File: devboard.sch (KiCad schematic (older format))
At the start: 101 parts, among them J1 Conn_01x04, J2 Conn_02x05_Odd_Even, J3 USB_B_Micro, J4 Conn_01x04, J5 Conn_02x10_Counter_Clockwise, J6 Conn_02x04_Counter_Clockwise, Q1 Q_NPN_BEC, Q2 Q_NPN_BEC, SW1 SW_SPST, U1 ATmega128L-8AU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

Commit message: Schematic cohesion improvements
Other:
- note added: "Daniel A. Stutman - 2021"
- note removed: "Daniel A. Stutman -2021"

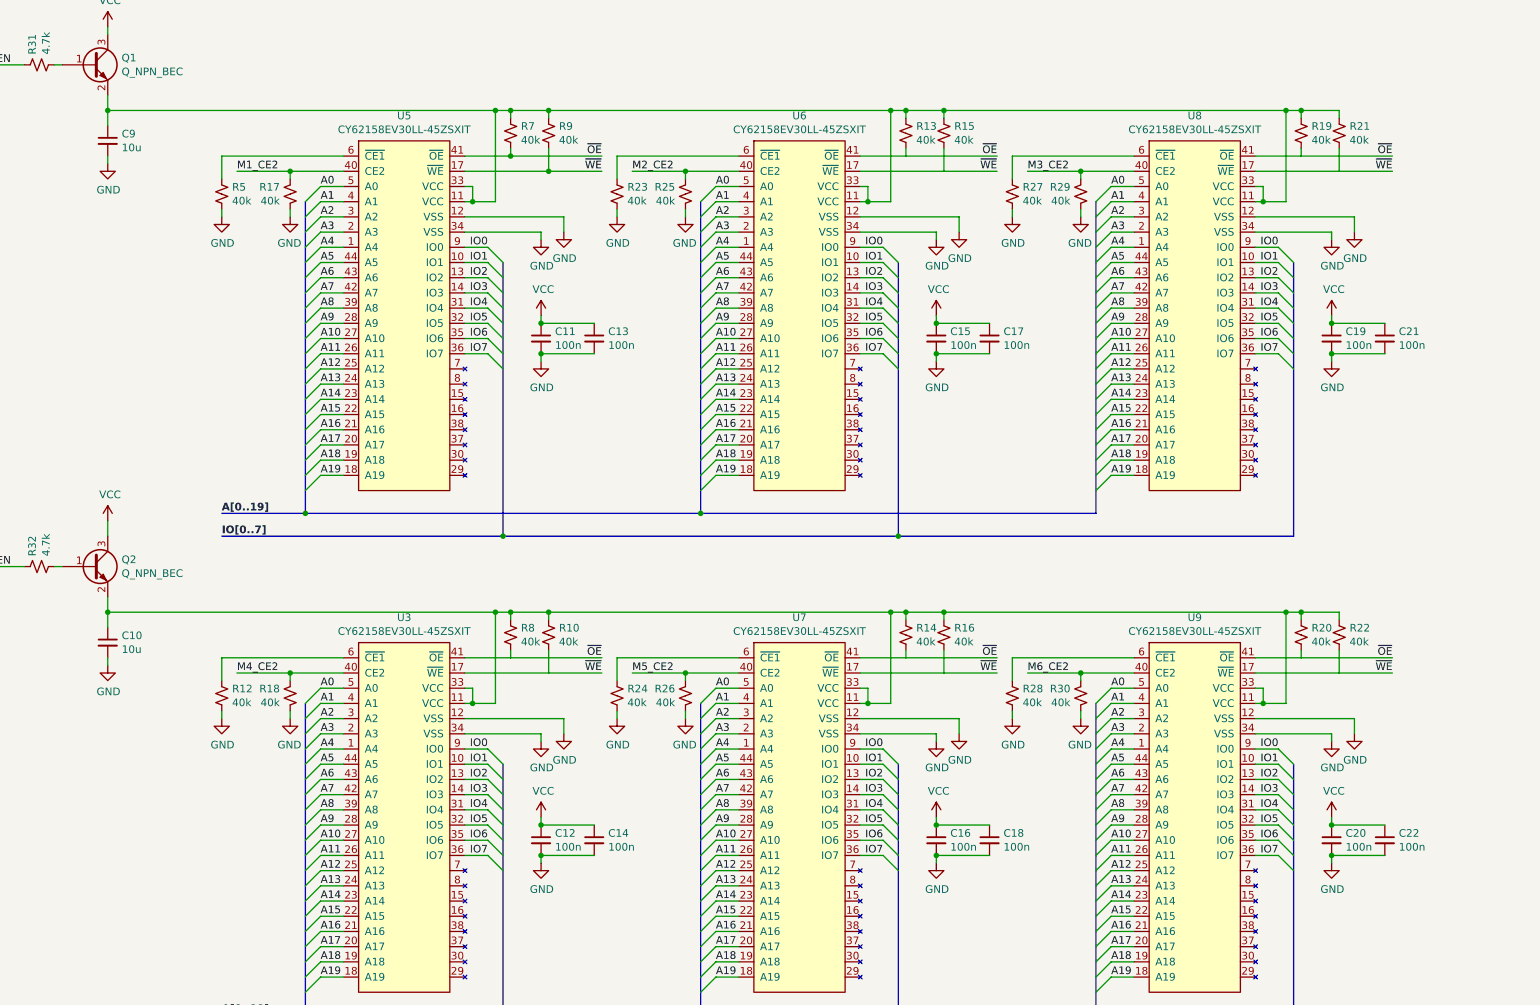
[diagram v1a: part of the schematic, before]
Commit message: Fix memory decoupling
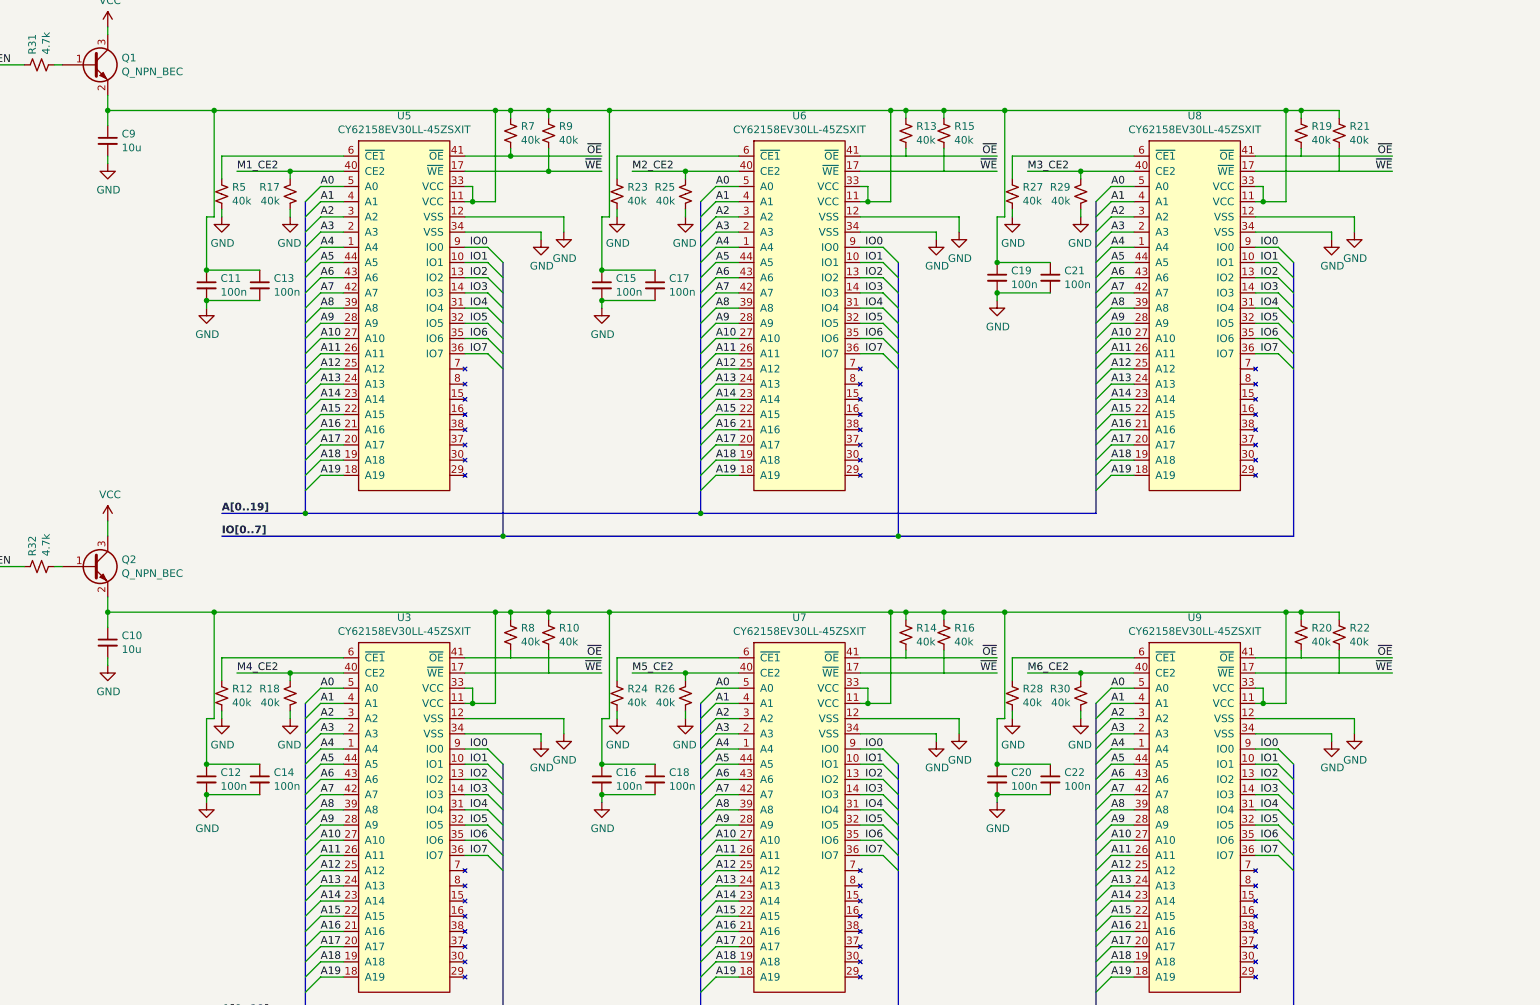
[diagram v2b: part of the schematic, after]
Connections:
- net VCC: no longer C11.1, C12.1, C13.1, C14.1, C15.1, C16.1, C17.1, C18.1, C19.1, C20.1, C21.1, C22.1
- net at C9.1, Q1.2 (E), R13.2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: now also C11.1, C13.1, C15.1, C17.1, C19.1, C21.1
- net at C10.1, Q2.2 (E), R10.2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: now also C12.1, C14.1, C16.1, C18.1, C20.1, C22.1
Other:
- moved on the sheet: C11, C12, C13, C14, C15, C16, C17, C18, C19, C20, C21, C22

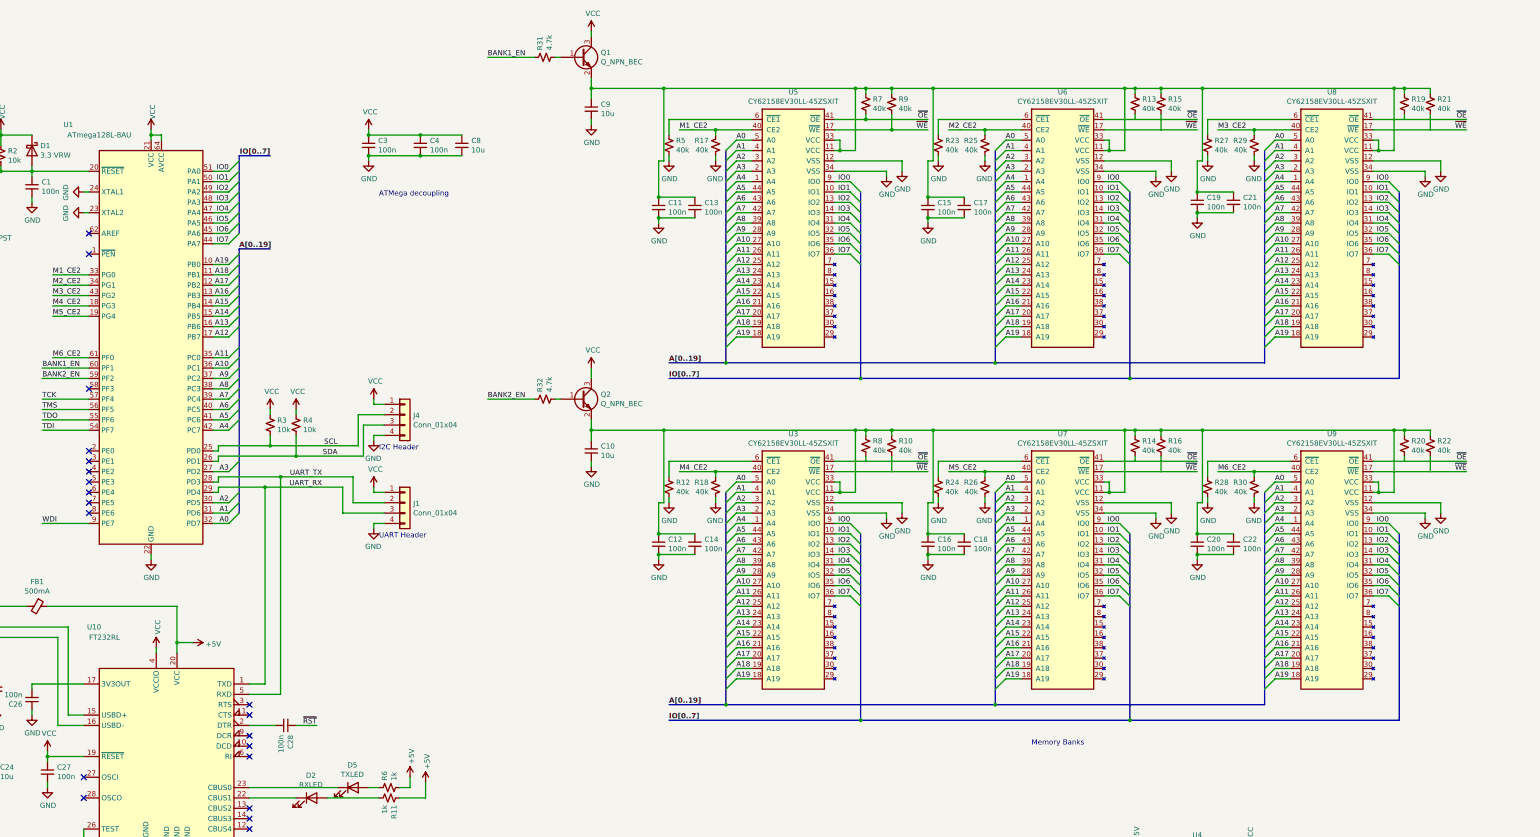
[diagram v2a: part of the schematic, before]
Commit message: Fix missing pin assignments and excessive pulls
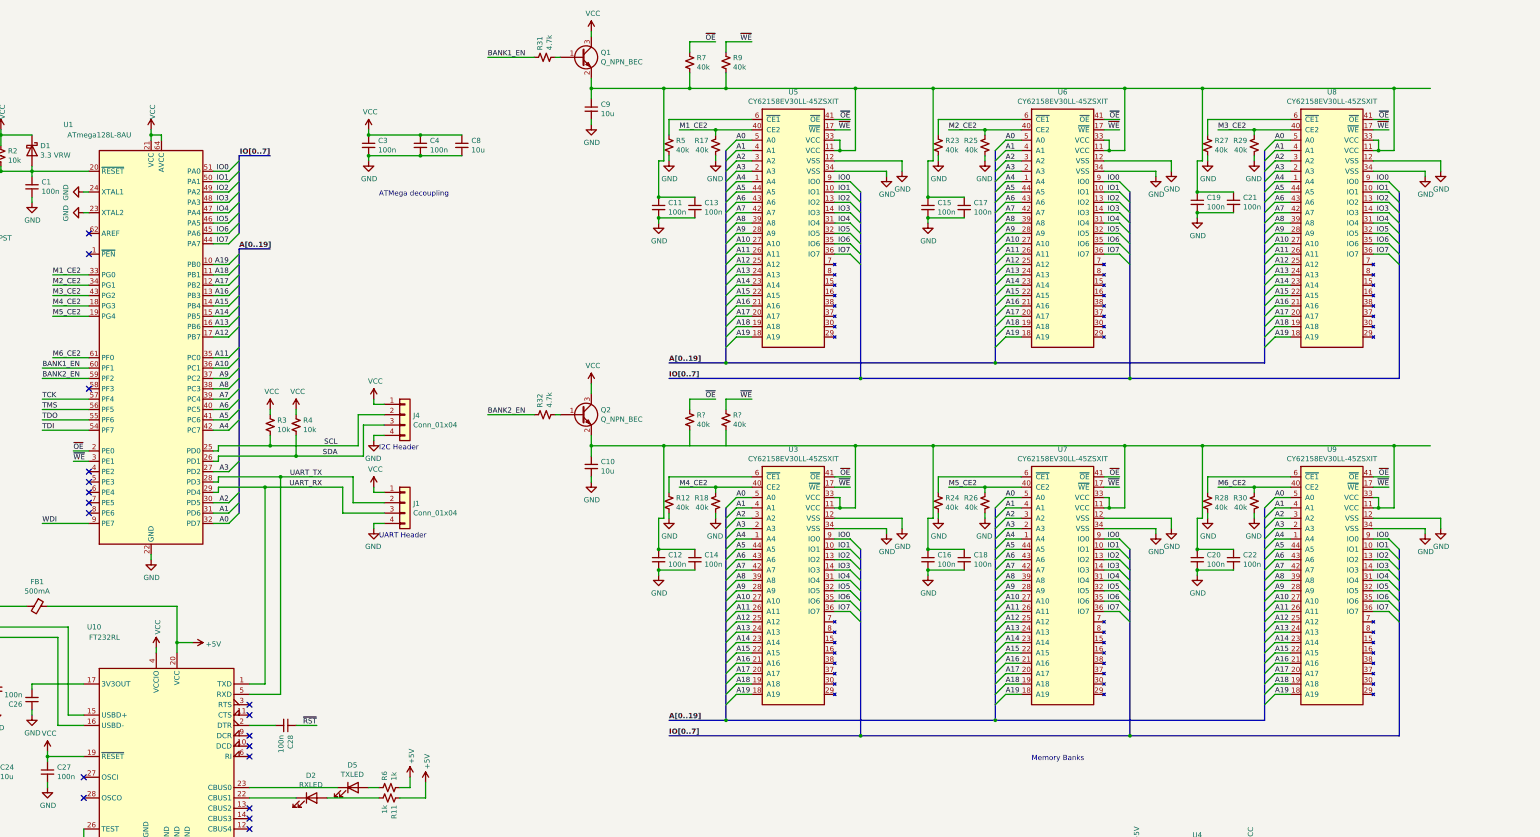
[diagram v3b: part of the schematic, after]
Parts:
- removed R10, R13, R14, R15, R16, R19, R20, R21, R22, R8: 40k, Resistor_SMD:R_0603_1608Metric_Pad0.98x0.95mm_HandSolder, symbol Device:R_Small_US
- added R? (x2): 40k, Resistor_SMD:R_0603_1608Metric_Pad0.98x0.95mm_HandSolder, symbol Device:R_Small_US
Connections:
- net ~OE: now also R7.2, U1.2 (PE0), R?.2; no longer R7.1
- net ~WE: now also R9.2, U1.3 (PE1), R?.2; no longer R9.1
- net at C11.1, C13.1, C15.1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: now also R7.1, R9.1; no longer R7.2, R9.2
- no-connect marks 23 -> 21
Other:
- moved on the sheet: C10, C12, C14, C16, C18, C20, C22, Q2, R12, R18, R24, R26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

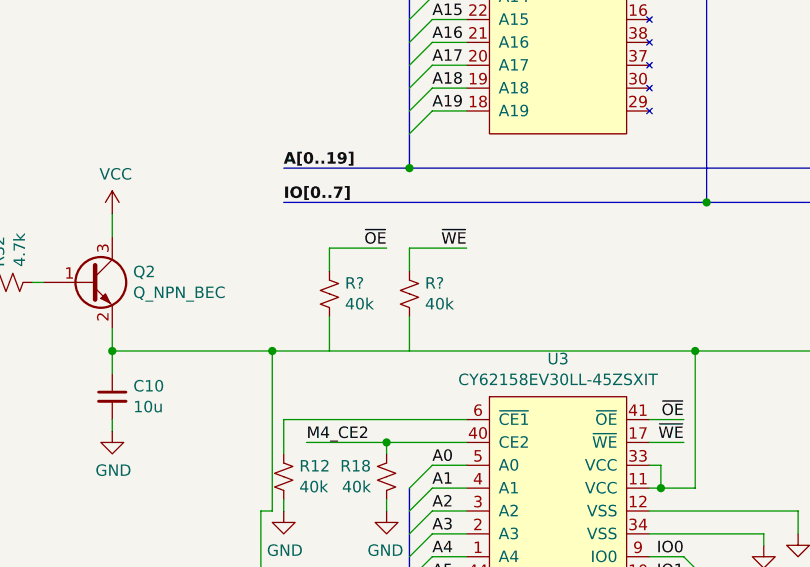
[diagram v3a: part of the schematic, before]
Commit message: Successfully route memories
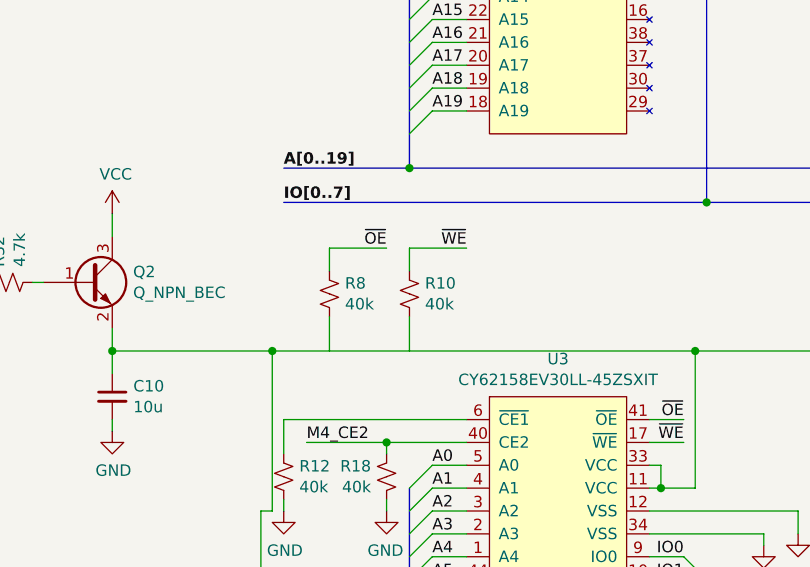
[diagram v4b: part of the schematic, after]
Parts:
- gave numbers to parts that had none: 2
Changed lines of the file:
@@
 	9250 1800 9400 1800
 $Comp
-L Device:R_Small_US R?
+L Device:R_Small_US R8
 U 1 1 6307DFC5
 P 7850 4600
-F 0 "R?" H 7782 4554 50  0000 R CNN
+F 0 "R8" H 7782 4554 50  0000 R CNN
 F 1 "40k" H 7782 4645 50  0000 R CNN
 F 2 "Resistor_SMD:R_0603_1608Metric_Pad0.98x0.95mm_HandSolder" H 7850 4600 50  0001 C CNN
@@
 $EndComp
 $Comp
-L Device:R_Small_US R?
+L Device:R_Small_US R10
 U 1 1 6307DFCB
 P 8200 4600
-F 0 "R?" H 8132 4554 50  0000 R CNN
+F 0 "R10" H 8132 4554 50  0000 R CNN
 F 1 "40k" H 8132 4645 50  0000 R CNN
 F 2 "Resistor_SMD:R_0603_1608Metric_Pad0.98x0.95mm_HandSolder" H 8200 4600 50  0001 C CNN

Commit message: Routing almost complete
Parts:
- removed C7: 100n, Capacitor_SMD:C_0603_1608Metric_Pad1.08x0.95mm_HandSolder, symbol Device:C_Small
- removed C8: 10u, Capacitor_SMD:C_0603_1608Metric_Pad1.08x0.95mm_HandSolder, symbol Device:C_Small
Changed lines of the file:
@@
 Text Label 650  2200 0    50   ~ 0
 ~RST
-Text Notes 4850 2450 0    50   ~ 0
+Text Notes 4650 2400 0    50   ~ 0
 ATMega decoupling
 Text Label 1600 4700 0    50   ~ 0
@@
 Wire Wire Line
 	3300 5250 3750 5250
-$Comp
-L Device:C_Small C8
-U 1 1 63A0F14D
-P 5650 1950
-F 0 "C8" H 5742 1996 50  0000 L CNN
-F 1 "10u" H 5742 1905 50  0000 L CNN
-F 2 "Capacitor_SMD:C_0603_1608Metric_Pad1.08x0.95mm_HandSolder" H 5650 1950 50  0001 C CNN
-F 3 "~" H 5650 1950 50  0001 C CNN
-	1    5650 1950
-	1    0    0    -1
-$EndComp
-Wire Wire Line
-	5250 1850 5650 1850
-Connection ~ 5250 1850
 Wire Wire Line
 	4750 2050 5250 2050
-Connection ~ 5250 2050
-Wire Wire Line
-	5250 2050 5650 2050
 $Comp
 L Connector:USB_B_Micro J3
@@
 Wire Wire Line
 	13250 8800 13250 8850
-Wire Wire Line
-	14750 9350 14750 9400
-Wire Wire Line
-	14550 9350 14750 9350
-$Comp
-L power:GND #PWR0121
-U 1 1 61D70742
-P 14750 9400
-F 0 "#PWR0121" H 14750 9150 50  0001 C CNN
-F 1 "GND" H 14755 9227 50  0000 C CNN
-F 2 "" H 14750 9400 50  0001 C CNN
-F 3 "" H 14750 9400 50  0001 C CNN
-	1    14750 9400
-	1    0    0    -1
-$EndComp
 Text Notes 12450 9550 0    50   ~ 0
 Supply Regulation
@@
 NoConn ~ 14550 9250
 $Comp
-L power:GND #PWR034
-U 1 1 5FE0A3E1
-P 15050 9300
-F 0 "#PWR034" H 15050 9050 50  0001 C CNN
-F 1 "GND" H 15055 9127 50  0000 C CNN
-F 2 "" H 15050 9300 50  0001 C CNN
-F 3 "" H 15050 9300 50  0001 C CNN
-	1    15050 9300
-	1    0    0    -1
-$EndComp
-$Comp
 L Connector_Generic:Conn_02x05_Odd_Even J2
 U 1 1 5FDF7679
@@
 Wire Wire Line
 	13100 9100 13100 9150
-$Comp
-L Device:C_Small C7
-U 1 1 5FE0A3D1
-P 15050 9150
-F 0 "C7" H 15142 9196 50  0000 L CNN
-F 1 "100n" H 15142 9105 50  0000 L CNN
-F 2 "Capacitor_SMD:C_0603_1608Metric_Pad1.08x0.95mm_HandSolder" H 15050 9150 50  0001 C CNN
-F 3 "~" H 15050 9150 50  0001 C CNN
-	1    15050 9150
-	1    0    0    -1
-$EndComp
-$Comp
-L power:VCC #PWR033
-U 1 1 5FE0A3D7
-P 15050 9000
-F 0 "#PWR033" H 15050 8850 50  0001 C CNN
-F 1 "VCC" H 15065 9173 50  0000 C CNN
-F 2 "" H 15050 9000 50  0001 C CNN
-F 3 "" H 15050 9000 50  0001 C CNN
-	1    15050 9000
-	1    0    0    -1
-$EndComp
-Wire Wire Line
-	15050 9000 15050 9050
-Wire Wire Line
-	15050 9300 15050 9250
 Wire Wire Line
 	2000 10200 2050 10200
@@
 Wire Wire Line
 	2050 5000 1900 5000
+$Comp
+L power:GND #PWR0121
+U 1 1 61D70742
+P 14750 9400
+F 0 "#PWR0121" H 14750 9150 50  0001 C CNN
+F 1 "GND" H 14755 9227 50  0000 C CNN
+F 2 "" H 14750 9400 50  0001 C CNN
+F 3 "" H 14750 9400 50  0001 C CNN
+	1    14750 9400
+	1    0    0    -1
+$EndComp
+Wire Wire Line
+	14550 9350 14750 9350
+Wire Wire Line
+	14750 9350 14750 9400
 Wire Bus Line
 	11700 10350 11700 10750

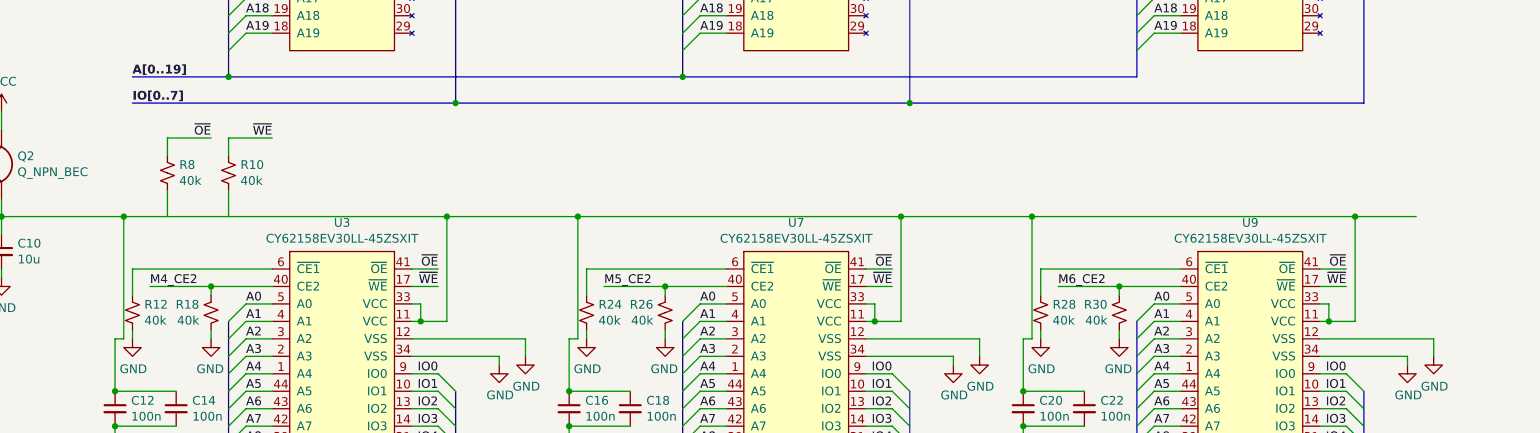
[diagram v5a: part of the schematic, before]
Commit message: Fix pullup connections and minor silk alterations
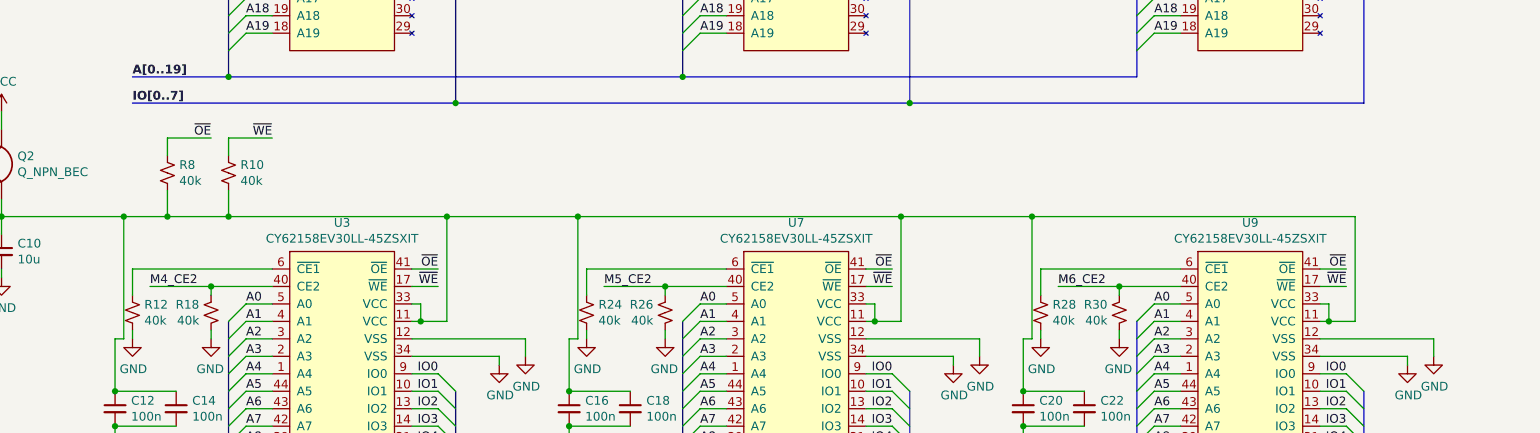
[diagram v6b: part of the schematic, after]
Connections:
- net at C10.1, C12.1, C14.1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: now also R10.1, R8.1
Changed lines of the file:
@@
 Wire Bus Line
 	10800 4050 13400 4050
-Connection ~ 14650 1400
 Wire Wire Line
 	14650 1400 14650 2000
@@
 	12050 1400 12800 1400
 Wire Wire Line
-	14650 1400 15000 1400
-Wire Wire Line
 	9450 1400 10200 1400
 Text Label 8450 950  2    50   ~ 0
@@
 Wire Bus Line
 	10800 7500 13400 7500
-Connection ~ 14650 4850
 Wire Wire Line
 	14500 5450 14650 5450
@@
 	7550 5550 7550 5850
 Wire Wire Line
-	7600 4850 9450 4850
+	7600 4850 7850 4850
 Wire Wire Line
 	10150 5550 10200 5550
@@
 Wire Wire Line
 	12050 4850 12800 4850
-Wire Wire Line
-	14650 4850 15000 4850
 Text Label 14600 5250 2    50   ~ 0
 ~WE
@@
 Wire Wire Line
 	8200 4400 8450 4400
-Wire Wire Line
-	7850 4700 7850 4850
-Wire Wire Line
-	8200 4700 8200 4850
 Text Label 1900 5000 0    50   ~ 0
 ~WE
@@
 Wire Wire Line
 	14750 9350 14750 9400
+Connection ~ 14650 1400
+Wire Wire Line
+	14650 1400 15000 1400
+Wire Wire Line
+	8200 4700 8200 4850
+Connection ~ 8200 4850
+Wire Wire Line
+	8200 4850 9450 4850
+Wire Wire Line
+	7850 4700 7850 4850
 Wire Bus Line
 	11700 10350 11700 10750
@@
 Wire Bus Line
 	8200 5450 8200 7500
+Connection ~ 7850 4850
+Wire Wire Line
+	7850 4850 8200 4850
 $EndSCHEMATC
